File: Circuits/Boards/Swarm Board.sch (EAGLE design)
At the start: 95 parts, among them CON1 ISP(2X3), T1 NPN2N2222, T10 TEFT4300, T11 NPN2N2222, T12 NPN2N2222, T13 NPN2N2222, T14 NPN2N2222, T15 NPN2N2222, T16 NPN2N2222, T17 NPN2N2222, T18 NPN2N2222, T2 NPN2N2222, T3 NPN2N2222, T4 TEFT4300, T5 TEFT4300, T6 TEFT4300, T7 TEFT4300, T8 TEFT4300, T9 TEFT4300, U1 ATMEGA324P, U2 MCP73832SOT-23, U3 TB6552FN/FNG

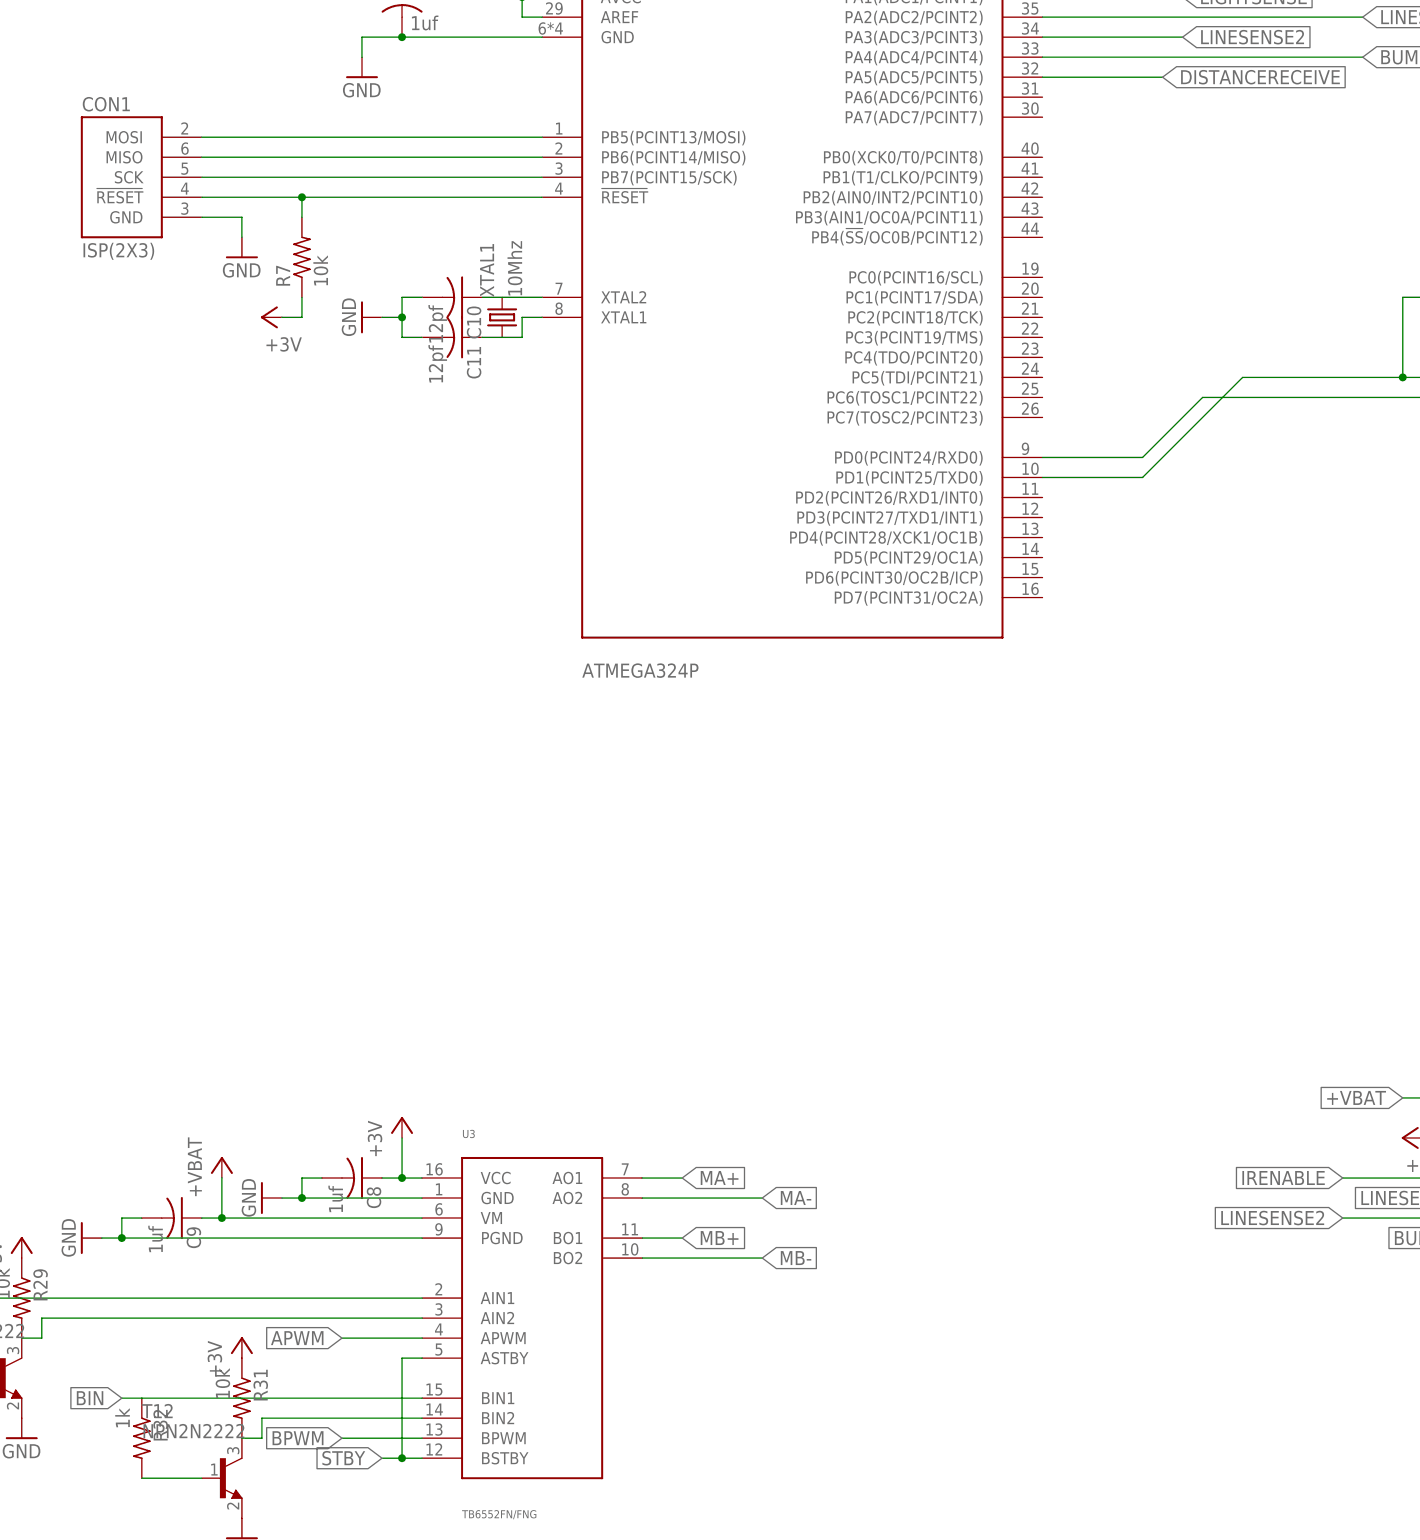
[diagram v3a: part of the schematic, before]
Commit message: 
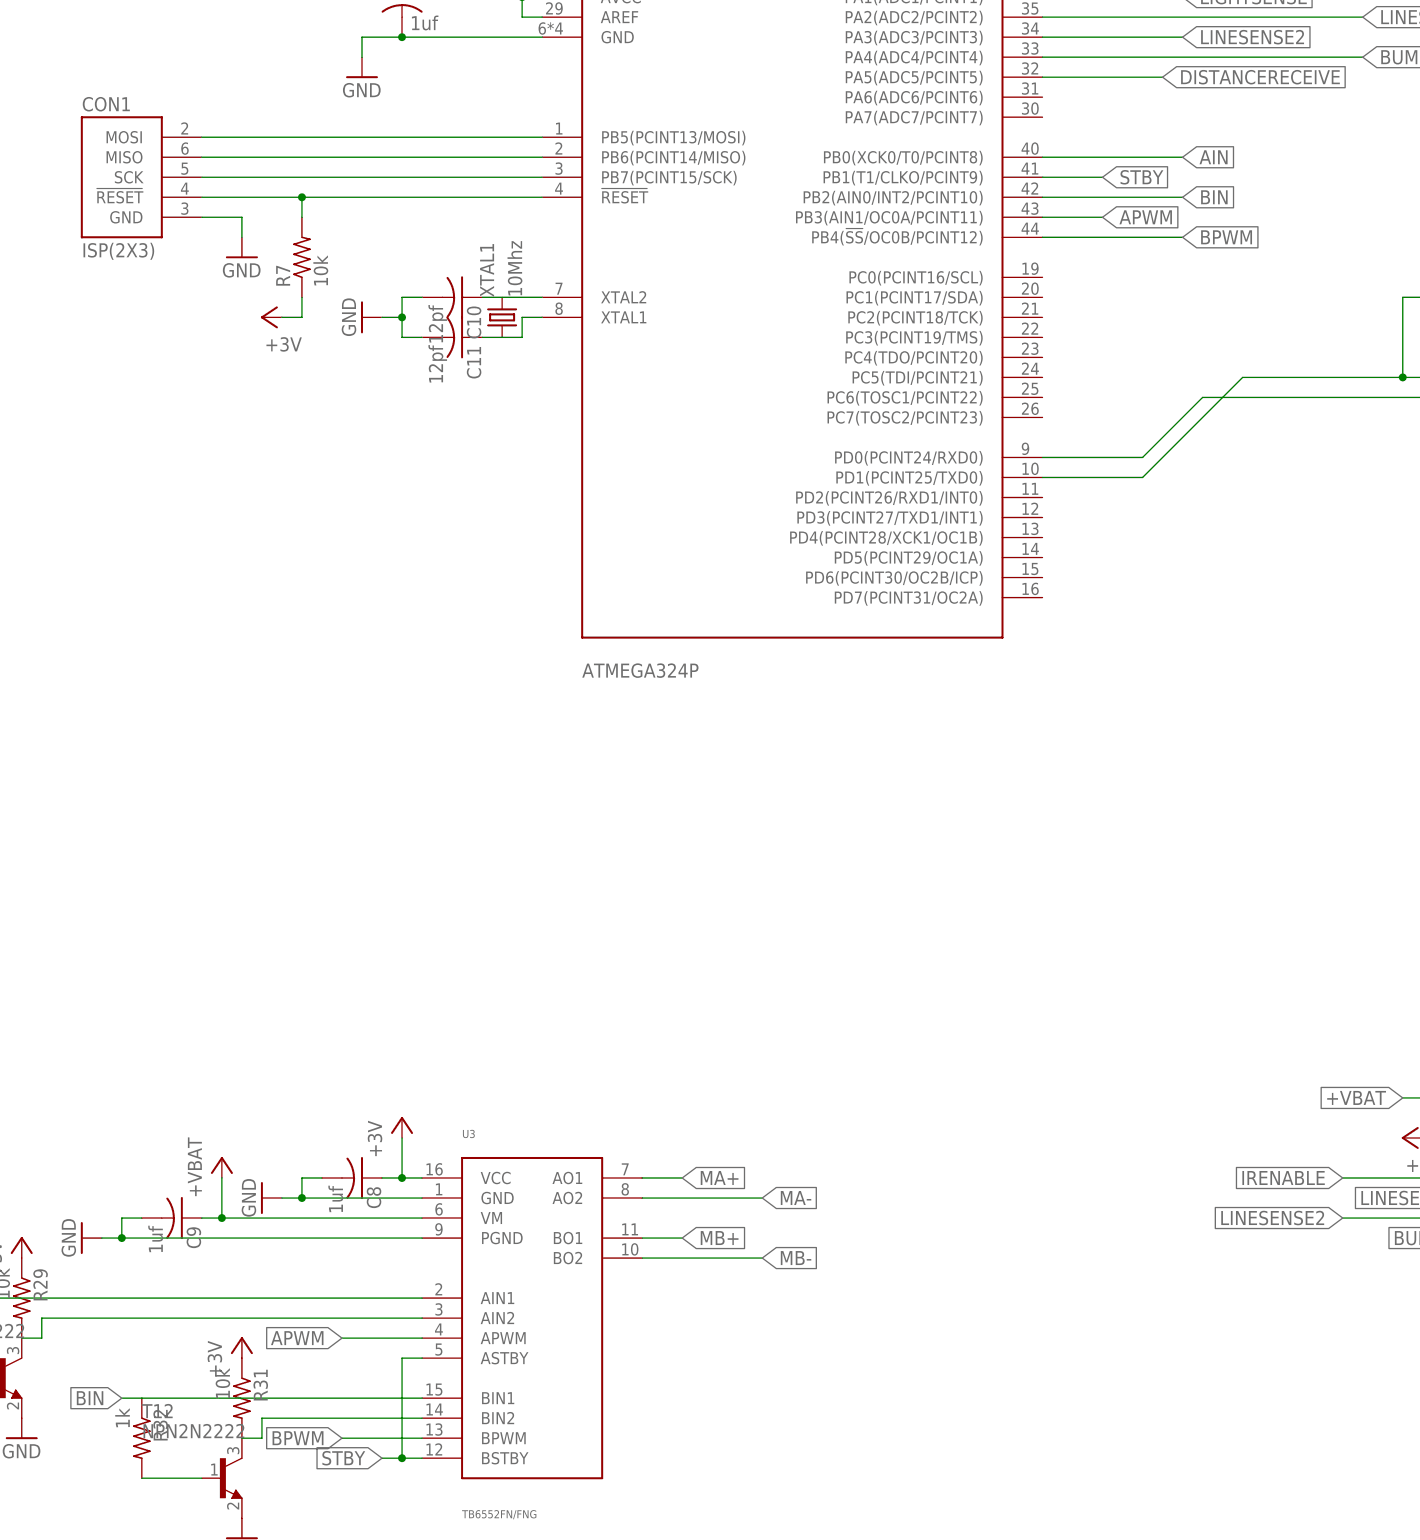
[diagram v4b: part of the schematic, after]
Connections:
- removed net AIN3: R31.2, T12.C
- net AIN: now also U1.PB0(XCK0/T0/PCINT8)
- net APWM: now also U1.PB3(AIN1/OC0A/PCINT11)
- net BIN: now also U1.PB2(AIN0/INT2/PCINT10)
- net BIN2: now also R31.2, T12.C
- net BPWM: now also U1.PB4(!SS!/OC0B/PCINT12)
- net STBY: now also U1.PB1(T1/CLKO/PCINT9)
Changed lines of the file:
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@@
 <label x="-53.34" y="-149.86" size="1.778" layer="91" rot="R180" xref="yes"/>
+</segment>
+<segment>
+<pinref part="U1" gate="G$1" pin="PB1(T1/CLKO/PCINT9)"/>
+<wire x1="30.48" y1="12.7" x2="38.1" y2="12.7" width="0.1524" layer="91"/>
+<label x="38.1" y="12.7" size="1.778" layer="91" xref="yes"/>
 </segment>
 </net>
@@
 <label x="-58.42" y="-147.32" size="1.778" layer="91" rot="R180" xref="yes"/>
 </segment>
-</net>
-<net name="BIN2" class="0">
-<segment>
-<pinref part="U3" gate="G$1" pin="BIN2"/>
-<wire x1="-48.26" y1="-144.78" x2="-68.58" y2="-144.78" width="0.1524" layer="91"/>
+<segment>
+<pinref part="U1" gate="G$1" pin="PB4(!SS!/OC0B/PCINT12)"/>
+<wire x1="30.48" y1="5.08" x2="48.26" y2="5.08" width="0.1524" layer="91"/>
+<label x="48.26" y="5.08" size="1.778" layer="91" xref="yes"/>
 </segment>
 </net>
 <net name="BIN" class="0">
 <segment>
-<pinref part="U3" gate="G$1" pin="BIN1"/>
-<wire x1="-48.26" y1="-142.24" x2="-83.82" y2="-142.24" width="0.1524" layer="91"/>
 <pinref part="R32" gate="G$1" pin="1"/>
 <wire x1="-83.82" y1="-142.24" x2="-86.36" y2="-142.24" width="0.1524" layer="91"/>
 <label x="-86.36" y="-142.24" size="1.778" layer="91" rot="R180" xref="yes"/>
+<pinref part="U3" gate="G$1" pin="BIN1"/>
+<wire x1="-83.82" y1="-142.24" x2="-48.26" y2="-142.24" width="0.1524" layer="91"/>
+</segment>
+<segment>
+<pinref part="U1" gate="G$1" pin="PB2(AIN0/INT2/PCINT10)"/>
+<wire x1="30.48" y1="10.16" x2="48.26" y2="10.16" width="0.1524" layer="91"/>
+<label x="48.26" y="10.16" size="1.778" layer="91" xref="yes"/>
 </segment>
 </net>
@@
 <wire x1="-48.26" y1="-134.62" x2="-58.42" y2="-134.62" width="0.1524" layer="91"/>
 <label x="-58.42" y="-134.62" size="1.778" layer="91" rot="R180" xref="yes"/>
+</segment>
+<segment>
+<pinref part="U1" gate="G$1" pin="PB3(AIN1/OC0A/PCINT11)"/>
+<wire x1="30.48" y1="7.62" x2="38.1" y2="7.62" width="0.1524" layer="91"/>
+<label x="38.1" y="7.62" size="1.778" layer="91" xref="yes"/>
 </segment>
 </net>
@@
 <pinref part="R30" gate="G$1" pin="1"/>
 <junction x="-111.76" y="-129.54"/>
+</segment>
+<segment>
+<pinref part="U1" gate="G$1" pin="PB0(XCK0/T0/PCINT8)"/>
+<wire x1="30.48" y1="15.24" x2="48.26" y2="15.24" width="0.1524" layer="91"/>
+<label x="48.26" y="15.24" size="1.778" layer="91" xref="yes"/>
 </segment>
 </net>
@@
 </segment>
 </net>
-<net name="AIN3" class="0">
+<net name="BIN2" class="0">
 <segment>
 <pinref part="T12" gate="G$1" pin="C"/>
@@
 <wire x1="-71.12" y1="-147.32" x2="-68.58" y2="-147.32" width="0.1524" layer="91"/>
 <wire x1="-68.58" y1="-147.32" x2="-68.58" y2="-144.78" width="0.1524" layer="91"/>
-</segment>
-</net>
+<pinref part="U3" gate="G$1" pin="BIN2"/>
+<wire x1="-48.26" y1="-144.78" x2="-68.58" y2="-144.78" width="0.1524" layer="91"/>
+</segment>
+</net>

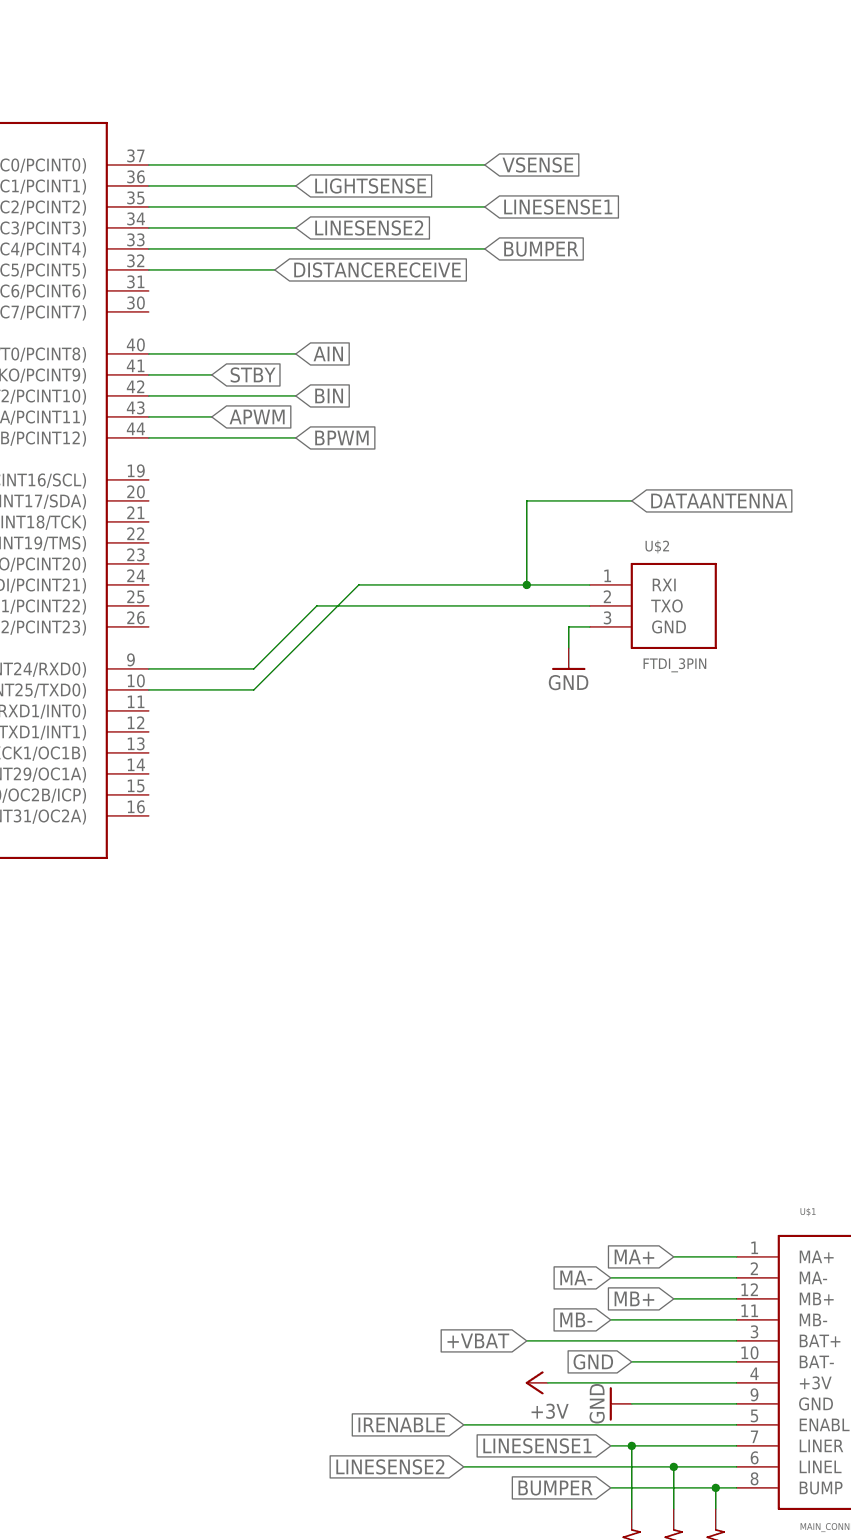
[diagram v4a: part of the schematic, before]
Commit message: 
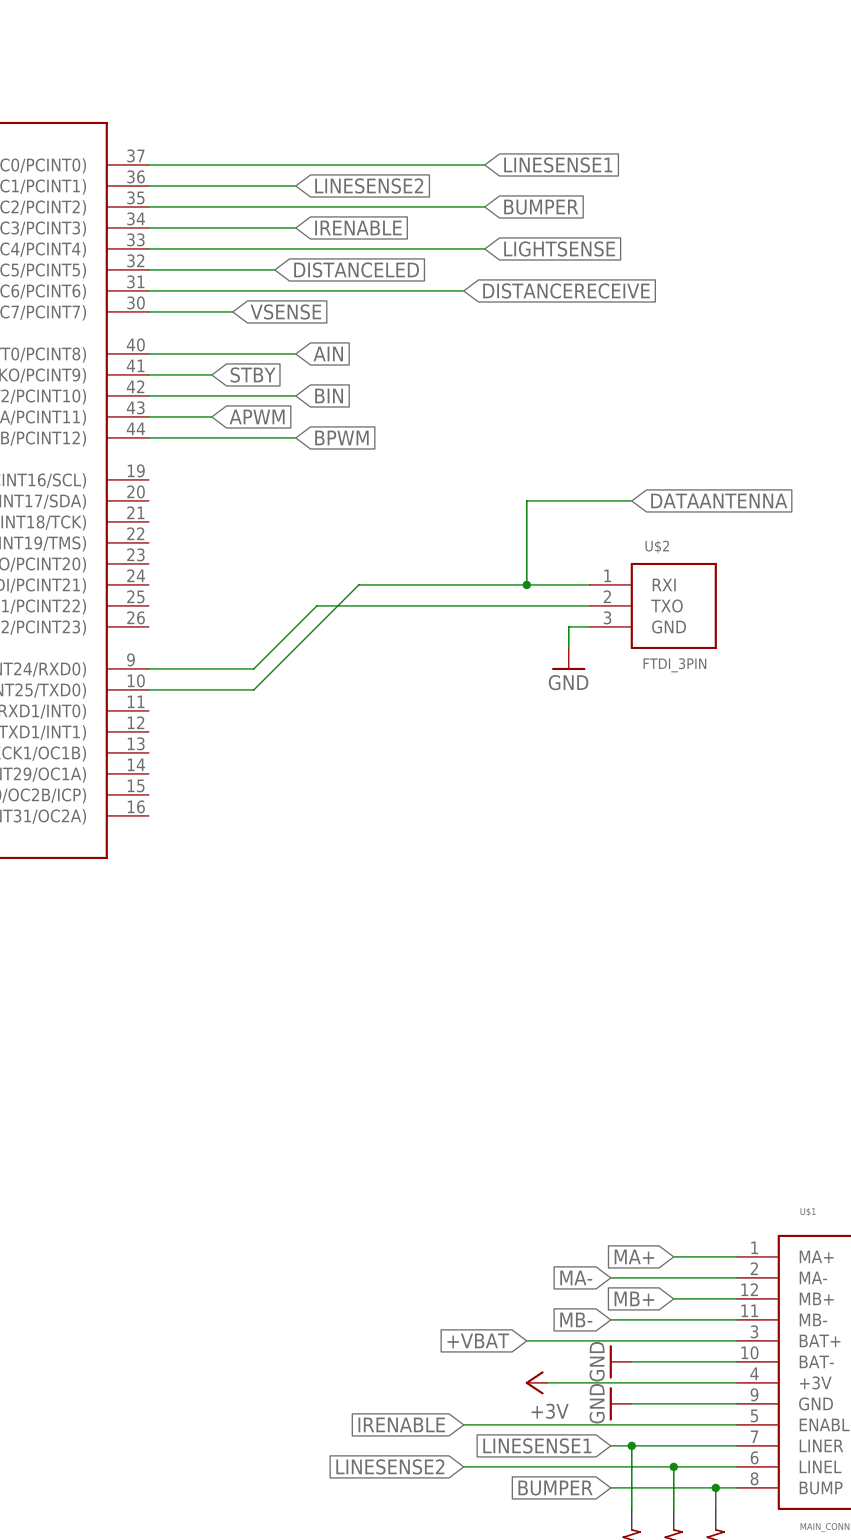
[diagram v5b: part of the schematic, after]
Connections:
- net BUMPER: now also U1.PA2(ADC2/PCINT2); no longer U1.PA4(ADC4/PCINT4)
- net DISTANCELED: now also U1.PA5(ADC5/PCINT5)
- net DISTANCERECEIVE: now also U1.PA6(ADC6/PCINT6); no longer U1.PA5(ADC5/PCINT5)
- net IRENABLE: now also U1.PA3(ADC3/PCINT3)
- net LIGHTSENSE: now also U1.PA4(ADC4/PCINT4); no longer U1.PA1(ADC1/PCINT1)
- net LINESENSE1: now also U1.PA0(ADC0/PCINT0); no longer U1.PA2(ADC2/PCINT2)
- net LINESENSE2: now also U1.PA1(ADC1/PCINT1); no longer U1.PA3(ADC3/PCINT3)
- net VSENSE: now also U1.PA7(ADC7/PCINT7); no longer U1.PA0(ADC0/PCINT0)
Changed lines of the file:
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@@
 <part name="R40" library="Passive" deviceset="RES" device="0603"/>
 <part name="R41" library="Passive" deviceset="RES" device="0603"/>
+<part name="GND28" library="Supply" deviceset="GND" device=""/>
 </parts>
 <sheets>
@@
 <instance part="R40" gate="G$1" x="381" y="96.52" rot="R90"/>
 <instance part="R41" gate="G$1" x="401.32" y="96.52" rot="R90"/>
+<instance part="GND28" gate="1" x="86.36" y="-106.68" rot="R270"/>
 </instances>
 <busses>
@@
 <pinref part="U$1" gate="G$1" pin="BAT-"/>
 <wire x1="101.6" y1="-106.68" x2="88.9" y2="-106.68" width="0.1524" layer="91"/>
-<label x="88.9" y="-106.68" size="1.778" layer="91" rot="R180" xref="yes"/>
+<pinref part="GND28" gate="1" pin="GND"/>
 </segment>
 <segment>
@@
 </segment>
 <segment>
-<pinref part="U1" gate="G$1" pin="PA0(ADC0/PCINT0)"/>
-<wire x1="30.48" y1="38.1" x2="71.12" y2="38.1" width="0.1524" layer="91"/>
-<label x="71.12" y="38.1" size="1.778" layer="91" xref="yes"/>
+<pinref part="U1" gate="G$1" pin="PA7(ADC7/PCINT7)"/>
+<wire x1="30.48" y1="20.32" x2="40.64" y2="20.32" width="0.1524" layer="91"/>
+<label x="40.64" y="20.32" size="1.778" layer="91" xref="yes"/>
 </segment>
 </net>
@@
 <net name="LIGHTSENSE" class="0">
 <segment>
-<pinref part="U1" gate="G$1" pin="PA1(ADC1/PCINT1)"/>
-<wire x1="30.48" y1="35.56" x2="48.26" y2="35.56" width="0.1524" layer="91"/>
-<label x="48.26" y="35.56" size="1.778" layer="91" xref="yes"/>
-</segment>
-<segment>
 <pinref part="PR1" gate="G$1" pin="1"/>
 <wire x1="-134.62" y1="-88.9" x2="-134.62" y2="-91.44" width="0.1524" layer="91"/>
@@
 <junction x="-134.62" y="-91.44"/>
 </segment>
+<segment>
+<pinref part="U1" gate="G$1" pin="PA4(ADC4/PCINT4)"/>
+<wire x1="30.48" y1="27.94" x2="71.12" y2="27.94" width="0.1524" layer="91"/>
+<label x="71.12" y="27.94" size="1.778" layer="91" xref="yes"/>
+</segment>
 </net>
 <net name="LINESENSE1" class="0">
-<segment>
-<pinref part="U1" gate="G$1" pin="PA2(ADC2/PCINT2)"/>
-<wire x1="30.48" y1="33.02" x2="71.12" y2="33.02" width="0.1524" layer="91"/>
-<label x="71.12" y="33.02" size="1.778" layer="91" xref="yes"/>
-</segment>
 <segment>
 <pinref part="U$1" gate="G$1" pin="LINER"/>
@@
 <pinref part="R33" gate="G$1" pin="2"/>
 </segment>
+<segment>
+<pinref part="U1" gate="G$1" pin="PA0(ADC0/PCINT0)"/>
+<wire x1="30.48" y1="38.1" x2="71.12" y2="38.1" width="0.1524" layer="91"/>
+<label x="71.12" y="38.1" size="1.778" layer="91" xref="yes"/>
+</segment>
 </net>
 <net name="LINESENSE2" class="0">
-<segment>
-<pinref part="U1" gate="G$1" pin="PA3(ADC3/PCINT3)"/>
-<wire x1="30.48" y1="30.48" x2="48.26" y2="30.48" width="0.1524" layer="91"/>
-<label x="48.26" y="30.48" size="1.778" layer="91" xref="yes"/>
-</segment>
 <segment>
 <pinref part="U$1" gate="G$1" pin="LINEL"/>
@@
 <junction x="93.98" y="-119.38"/>
 <pinref part="R34" gate="G$1" pin="2"/>
+</segment>
+<segment>
+<pinref part="U1" gate="G$1" pin="PA1(ADC1/PCINT1)"/>
+<wire x1="30.48" y1="35.56" x2="48.26" y2="35.56" width="0.1524" layer="91"/>
+<label x="48.26" y="35.56" size="1.778" layer="91" xref="yes"/>
 </segment>
 </net>
@@
 <label x="175.26" y="-40.64" size="1.778" layer="91" rot="R180" xref="yes"/>
 </segment>
+<segment>
+<pinref part="U1" gate="G$1" pin="PA5(ADC5/PCINT5)"/>
+<wire x1="30.48" y1="25.4" x2="45.72" y2="25.4" width="0.1524" layer="91"/>
+<label x="45.72" y="25.4" size="1.778" layer="91" xref="yes"/>
+</segment>
 </net>
 <net name="STBY" class="0">
@@
 </segment>
 <segment>
-<pinref part="U1" gate="G$1" pin="PA5(ADC5/PCINT5)"/>
-<wire x1="30.48" y1="25.4" x2="45.72" y2="25.4" width="0.1524" layer="91"/>
-<label x="45.72" y="25.4" size="1.778" layer="91" xref="yes"/>
+<pinref part="U1" gate="G$1" pin="PA6(ADC6/PCINT6)"/>
+<wire x1="30.48" y1="22.86" x2="68.58" y2="22.86" width="0.1524" layer="91"/>
+<label x="68.58" y="22.86" size="1.778" layer="91" xref="yes"/>
 </segment>
 </net>
@@
 <wire x1="101.6" y1="-114.3" x2="68.58" y2="-114.3" width="0.1524" layer="91"/>
 <label x="68.58" y="-114.3" size="1.778" layer="91" rot="R180" xref="yes"/>
+</segment>
+<segment>
+<pinref part="U1" gate="G$1" pin="PA3(ADC3/PCINT3)"/>
+<wire x1="30.48" y1="30.48" x2="48.26" y2="30.48" width="0.1524" layer="91"/>
+<label x="48.26" y="30.48" size="1.778" layer="91" xref="yes"/>
 </segment>
 </net>
@@
 </segment>
 <segment>
-<pinref part="U1" gate="G$1" pin="PA4(ADC4/PCINT4)"/>
-<wire x1="30.48" y1="27.94" x2="71.12" y2="27.94" width="0.1524" layer="91"/>
-<label x="71.12" y="27.94" size="1.778" layer="91" xref="yes"/>
-</segment>
-</net>
+<pinref part="U1" gate="G$1" pin="PA2(ADC2/PCINT2)"/>
+<wire x1="30.48" y1="33.02" x2="71.12" y2="33.02" width="0.1524" layer="91"/>
+<label x="71.12" y="33.02" size="1.778" layer="91" xref="yes"/>
+</segment>
+</net>
